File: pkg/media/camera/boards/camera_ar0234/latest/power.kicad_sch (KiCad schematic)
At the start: 17 parts, among them U2 ATtiny402-SS, U3 LP5907MFX-2.8, U4 TLV74318PDBVR, U5 TLV75512PDYDR

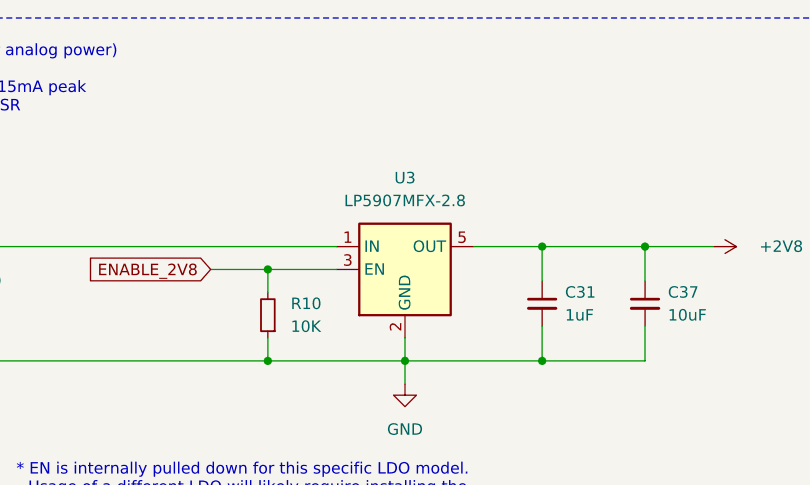
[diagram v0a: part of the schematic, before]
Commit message: Mocap tweaks and add CM4 support with SDCard.
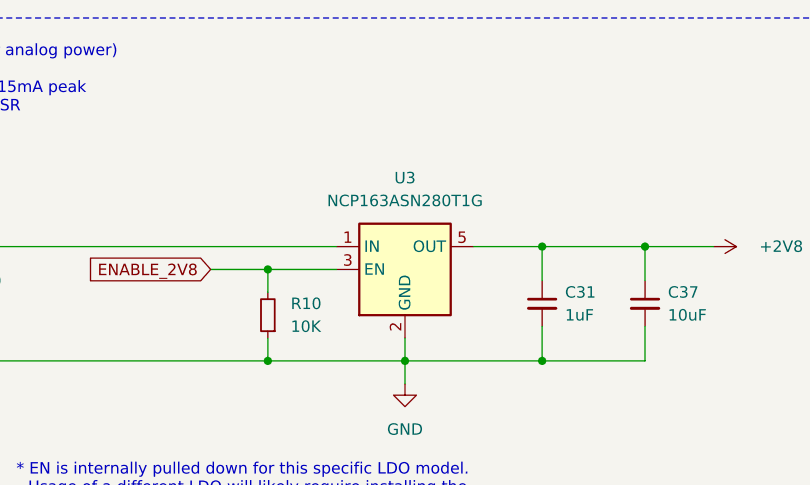
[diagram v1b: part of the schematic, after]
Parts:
- U3: value LP5907MFX-2.8 -> NCP163ASN280T1G
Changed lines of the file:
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@@
 			)
 		)
-		(property "Value" "LP5907MFX-2.8"
+		(property "Value" "NCP163ASN280T1G"
 			(at 82.55 35.56 0)
 			(effects
@@
 			)
 		)
-		(property "Datasheet" "http://www.ti.com/lit/ds/symlink/lp5907.pdf"
+		(property "Datasheet" ""
 			(at 82.55 30.48 0)
 			(effects
@@
 			)
 		)
-		(property "Description" "250-mA Ultra-Low-Noise Low-IQ LDO, 2.8V, SOT-23"
+		(property "Description" ""
 			(at 82.55 43.18 0)
 			(effects
